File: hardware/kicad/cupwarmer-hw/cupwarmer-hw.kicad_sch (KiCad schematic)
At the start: 3 parts

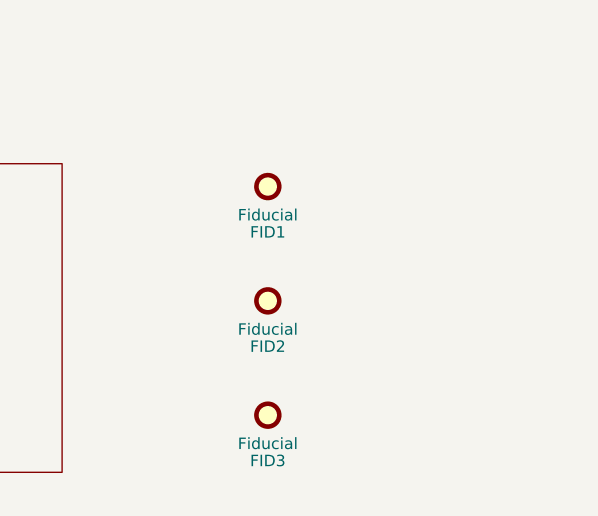
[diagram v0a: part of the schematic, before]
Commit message: Fix DRC: link mounting holes to schematic and custom footprint
Add Mechanical:MountingHole symbols H1/H2 to the top-level schematic so
the PCB mounting holes are no longer flagged as extra_footprint by DRC.
Add a custom cupwarmer:MountingHole_M2_Plastic_D2.4mm footprint to the
project library and point both PCB footprints at it so the lib copy
matches the in-board geometry. Align Value and Description fields
between schematic and PCB.

Co-Authored-By: Claude Opus 4.7 (1M context) <noreply@anthropic.com>
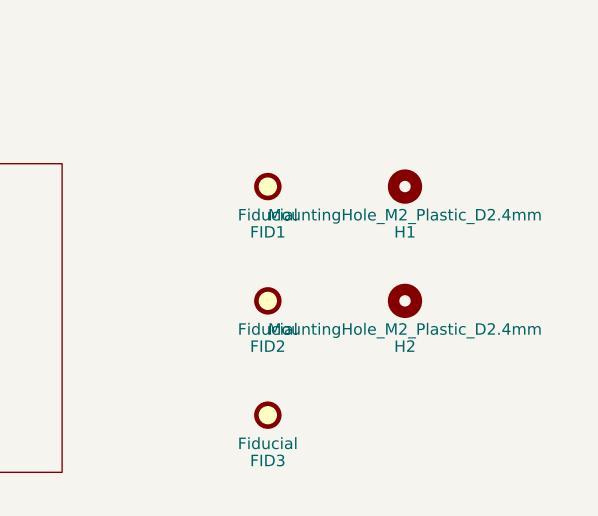
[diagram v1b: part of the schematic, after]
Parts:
- added H1, H2: MountingHole_M2_Plastic_D2.4mm, cupwarmer:MountingHole_M2_Plastic_D2.4mm, symbol Mechanical:MountingHole
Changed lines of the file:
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@@
 		(comment 3 "15W Qi Cup Warmer")
+	)
+	(symbol
+		(lib_id "Mechanical:MountingHole")
+		(at 195.58 46.99 0)
+		(unit 1)
+		(body_style 1)
+		(exclude_from_sim no)
+		(in_bom no)
+		(on_board yes)
+		(in_pos_files yes)
+		(dnp no)
+		(property "Reference" "H1"
+			(at 195.58 52.07 0)
+			(show_name no)
+			(do_not_autoplace no)
+			(effects
+				(font
+					(size 1.27 1.27)
+				)
+			)
+		)
+		(property "Value" "MountingHole_M2_Plastic_D2.4mm"
+			(at 195.58 50.165 0)
+			(show_name no)
+			(do_not_autoplace no)
+			(effects
+				(font
+					(size 1.27 1.27)
+				)
+			)
+		)
+		(property "Footprint" "cupwarmer:MountingHole_M2_Plastic_D2.4mm"
+			(at 195.58 46.99 0)
+			(hide yes)
+			(show_name no)
+			(do_not_autoplace no)
+			(effects
+				(font
+					(size 1.27 1.27)
+				)
+			)
+		)
+		(property "Datasheet" ""
+			(at 195.58 46.99 0)
+			(hide yes)
+			(show_name no)
+			(do_not_autoplace no)
+			(effects
+				(font
+					(size 1.27 1.27)
+				)
+			)
+		)
+		(property "Description" "Mounting Hole without connection"
+			(at 195.58 46.99 0)
+			(hide yes)
+			(show_name no)
+			(do_not_autoplace no)
+			(effects
+				(font
+					(size 1.27 1.27)
+				)
+			)
+		)
+		(instances
+			(project "cupwarmer-hw"
+				(path "/f3c63676-f392-4700-9f58-a6787e1eb284"
+					(reference "H1")
+					(unit 1)
+				)
+			)
+		)
+	)
+	(symbol
+		(lib_id "Mechanical:MountingHole")
+		(at 195.58 59.69 0)
+		(unit 1)
+		(body_style 1)
+		(exclude_from_sim no)
+		(in_bom no)
+		(on_board yes)
+		(in_pos_files yes)
+		(dnp no)
+		(property "Reference" "H2"
+			(at 195.58 64.77 0)
+			(show_name no)
+			(do_not_autoplace no)
+			(effects
+				(font
+					(size 1.27 1.27)
+				)
+			)
+		)
+		(property "Value" "MountingHole_M2_Plastic_D2.4mm"
+			(at 195.58 62.865 0)
+			(show_name no)
+			(do_not_autoplace no)
+			(effects
+				(font
+					(size 1.27 1.27)
+				)
+			)
+		)
+		(property "Footprint" "cupwarmer:MountingHole_M2_Plastic_D2.4mm"
+			(at 195.58 59.69 0)
+			(hide yes)
+			(show_name no)
+			(do_not_autoplace no)
+			(effects
+				(font
+					(size 1.27 1.27)
+				)
+			)
+		)
+		(property "Datasheet" ""
+			(at 195.58 59.69 0)
+			(hide yes)
+			(show_name no)
+			(do_not_autoplace no)
+			(effects
+				(font
+					(size 1.27 1.27)
+				)
+			)
+		)
+		(property "Description" "Mounting Hole without connection"
+			(at 195.58 59.69 0)
+			(hide yes)
+			(show_name no)
+			(do_not_autoplace no)
+			(effects
+				(font
+					(size 1.27 1.27)
+				)
+			)
+		)
+		(instances
+			(project "cupwarmer-hw"
+				(path "/f3c63676-f392-4700-9f58-a6787e1eb284"
+					(reference "H2")
+					(unit 1)
+				)
+			)
+		)
 	)
 	(text "Top-level hierarchical structure"

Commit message: Reposition mounting hole symbols and save KiCad UI state
Co-Authored-By: Claude Opus 4.7 (1M context) <noreply@anthropic.com>
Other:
- moved on the sheet: H1, H2
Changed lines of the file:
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@@
 		(comment 3 "15W Qi Cup Warmer")
-	)
-	(symbol
-		(lib_id "Mechanical:MountingHole")
-		(at 195.58 46.99 0)
-		(unit 1)
-		(body_style 1)
-		(exclude_from_sim no)
-		(in_bom no)
-		(on_board yes)
-		(in_pos_files yes)
-		(dnp no)
-		(property "Reference" "H1"
-			(at 195.58 52.07 0)
-			(show_name no)
-			(do_not_autoplace no)
-			(effects
-				(font
-					(size 1.27 1.27)
-				)
-			)
-		)
-		(property "Value" "MountingHole_M2_Plastic_D2.4mm"
-			(at 195.58 50.165 0)
-			(show_name no)
-			(do_not_autoplace no)
-			(effects
-				(font
-					(size 1.27 1.27)
-				)
-			)
-		)
-		(property "Footprint" "cupwarmer:MountingHole_M2_Plastic_D2.4mm"
-			(at 195.58 46.99 0)
-			(hide yes)
-			(show_name no)
-			(do_not_autoplace no)
-			(effects
-				(font
-					(size 1.27 1.27)
-				)
-			)
-		)
-		(property "Datasheet" ""
-			(at 195.58 46.99 0)
-			(hide yes)
-			(show_name no)
-			(do_not_autoplace no)
-			(effects
-				(font
-					(size 1.27 1.27)
-				)
-			)
-		)
-		(property "Description" "Mounting Hole without connection"
-			(at 195.58 46.99 0)
-			(hide yes)
-			(show_name no)
-			(do_not_autoplace no)
-			(effects
-				(font
-					(size 1.27 1.27)
-				)
-			)
-		)
-		(instances
-			(project "cupwarmer-hw"
-				(path "/f3c63676-f392-4700-9f58-a6787e1eb284"
-					(reference "H1")
-					(unit 1)
-				)
-			)
-		)
-	)
-	(symbol
-		(lib_id "Mechanical:MountingHole")
-		(at 195.58 59.69 0)
-		(unit 1)
-		(body_style 1)
-		(exclude_from_sim no)
-		(in_bom no)
-		(on_board yes)
-		(in_pos_files yes)
-		(dnp no)
-		(property "Reference" "H2"
-			(at 195.58 64.77 0)
-			(show_name no)
-			(do_not_autoplace no)
-			(effects
-				(font
-					(size 1.27 1.27)
-				)
-			)
-		)
-		(property "Value" "MountingHole_M2_Plastic_D2.4mm"
-			(at 195.58 62.865 0)
-			(show_name no)
-			(do_not_autoplace no)
-			(effects
-				(font
-					(size 1.27 1.27)
-				)
-			)
-		)
-		(property "Footprint" "cupwarmer:MountingHole_M2_Plastic_D2.4mm"
-			(at 195.58 59.69 0)
-			(hide yes)
-			(show_name no)
-			(do_not_autoplace no)
-			(effects
-				(font
-					(size 1.27 1.27)
-				)
-			)
-		)
-		(property "Datasheet" ""
-			(at 195.58 59.69 0)
-			(hide yes)
-			(show_name no)
-			(do_not_autoplace no)
-			(effects
-				(font
-					(size 1.27 1.27)
-				)
-			)
-		)
-		(property "Description" "Mounting Hole without connection"
-			(at 195.58 59.69 0)
-			(hide yes)
-			(show_name no)
-			(do_not_autoplace no)
-			(effects
-				(font
-					(size 1.27 1.27)
-				)
-			)
-		)
-		(instances
-			(project "cupwarmer-hw"
-				(path "/f3c63676-f392-4700-9f58-a6787e1eb284"
-					(reference "H2")
-					(unit 1)
-				)
-			)
-		)
 	)
 	(text "Top-level hierarchical structure"
@@
 					(unit 1)
 				)
+			)
+		)
+	)
+	(symbol
+		(lib_id "Mechanical:MountingHole")
+		(at 203.2 46.99 0)
+		(unit 1)
+		(body_style 1)
+		(exclude_from_sim no)
+		(in_bom no)
+		(on_board yes)
+		(in_pos_files yes)
+		(dnp no)
+		(property "Reference" "H1"
+			(at 203.2 52.07 0)
+			(show_name no)
+			(do_not_autoplace no)
+			(effects
+				(font
+					(size 1.27 1.27)
+				)
+			)
+		)
+		(property "Value" "MountingHole_M2_Plastic_D2.4mm"
+			(at 203.2 50.165 0)
+			(show_name no)
+			(do_not_autoplace no)
+			(effects
+				(font
+					(size 1.27 1.27)
+				)
+			)
+		)
+		(property "Footprint" "cupwarmer:MountingHole_M2_Plastic_D2.4mm"
+			(at 203.2 46.99 0)
+			(hide yes)
+			(show_name no)
+			(do_not_autoplace no)
+			(effects
+				(font
+					(size 1.27 1.27)
+				)
+			)
+		)
+		(property "Datasheet" ""
+			(at 203.2 46.99 0)
+			(hide yes)
+			(show_name no)
+			(do_not_autoplace no)
+			(effects
+				(font
+					(size 1.27 1.27)
+				)
+			)
+		)
+		(property "Description" "Mounting Hole without connection"
+			(at 203.2 46.99 0)
+			(hide yes)
+			(show_name no)
+			(do_not_autoplace no)
+			(effects
+				(font
+					(size 1.27 1.27)
+				)
+			)
+		)
+		(instances
+			(project "cupwarmer-hw"
+				(path "/f3c63676-f392-4700-9f58-a6787e1eb284"
+					(reference "H1")
+					(unit 1)
+				)
+			)
+		)
+	)
+	(symbol
+		(lib_id "Mechanical:MountingHole")
+		(at 203.2 59.69 0)
+		(unit 1)
+		(body_style 1)
+		(exclude_from_sim no)
+		(in_bom no)
+		(on_board yes)
+		(in_pos_files yes)
+		(dnp no)
+		(property "Reference" "H2"
+			(at 203.2 64.77 0)
+			(show_name no)
+			(do_not_autoplace no)
+			(effects
+				(font
+					(size 1.27 1.27)
+				)
+			)
+		)
+		(property "Value" "MountingHole_M2_Plastic_D2.4mm"
+			(at 203.2 62.865 0)
+			(show_name no)
+			(do_not_autoplace no)
+			(effects
+				(font
+					(size 1.27 1.27)
+				)
+			)
+		)
+		(property "Footprint" "cupwarmer:MountingHole_M2_Plastic_D2.4mm"
+			(at 203.2 59.69 0)
+			(hide yes)
+			(show_name no)
+			(do_not_autoplace no)
+			(effects
+				(font
+					(size 1.27 1.27)
+				)
+			)
+		)
+		(property "Datasheet" ""
+			(at 203.2 59.69 0)
+			(hide yes)
+			(show_name no)
+			(do_not_autoplace no)
+			(effects
+				(font
+					(size 1.27 1.27)
+				)
+			)
+		)
+		(property "Description" "Mounting Hole without connection"
+			(at 203.2 59.69 0)
+			(hide yes)
+			(show_name no)
+			(do_not_autoplace no)
+			(effects
+				(font
+					(size 1.27 1.27)
+				)
+			)
+		)
+		(instances
+			(project "cupwarmer-hw"
+				(path "/f3c63676-f392-4700-9f58-a6787e1eb284"
+					(reference "H2")
+					(unit 1)
+				)
